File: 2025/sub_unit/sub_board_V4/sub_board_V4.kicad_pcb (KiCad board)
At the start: 2 copper layers, 66.8 x 58 mm, 38 parts, among them J1 Conn_01x02_Socket, J10 Conn_01x02_Socket, J11 Conn_01x03_Socket, J12 Conn_01x02_Socket, J13 Conn_01x02_Socket, J14 Conn_01x05_Socket, J15 Conn_01x05_Socket, J16 Conn_01x02_Socket, J18 Conn_01x07_Socket, J19 Conn_01x07_Socket, J2 Conn_01x02_Socket, J3 Conn_01x02_Socket, J4 Conn_01x02_Socket, J5 Conn_01x02_Socket, J6 Conn_01x02_Socket, J7 Conn_01x02_Socket, J8 Conn_01x02_Socket, J9 Conn_01x02_Socket

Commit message: 回路図変更
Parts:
- added J17: Conn_01x02_Socket, Connector_JST:JST_PH_B2B-PH-K_1x02_P2.00mm_Vertical, F.Cu at (25.6, -15.3)
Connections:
- J11 pad 1: DRI_SIGNAL -> GNDPWR
- J11 pad 3: GNDPWR -> +6V
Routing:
- net DRI_SIGNAL: track 59.3 -> 0.01 mm
- net GNDPWR: track 16.6 -> 24.1 mm
- net +6V: track 141.3 -> 147.8 mm

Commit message: PCB修正
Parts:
- moved J17 8.64 mm to (18.4, -10.7)
- moved D1 5.63 mm to (19.9, -18.8)
- moved R3 5.51 mm to (14.4, -16.2), turned to 0 degrees
- moved D2 5.42 mm to (19.9, -20.6)
- moved R1 3.10 mm to (14.3, -20.6)
- moved R4 3.08 mm to (14.3, -18.8)
- moved G*** 0.89 mm to (17.2, -17.4)
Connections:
- J19 pad 3: DRI_SIGNAL -> unconnected-(J19-Pin_3-Pad3)
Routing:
- net CANH: track 109.8 -> 131.7 mm
- net CANL: track 111.5 -> 130.8 mm
- net +6V: track 147.8 -> 160.9 mm
- net GNDPWR: track 24.1 -> 20.4 mm
- net Net-(D1-A): track 2.05 -> 5.03 mm
- net Net-(J13-Pin_1): track 8.80 -> 5.89 mm
- net Net-(D2-A): track 1.94 -> 4.73 mm
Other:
- board text added: "+15"
- board text added: "+6"
- board text added: "V4.0"
- board text removed: "+15V"
- board text removed: "+6V"
- board text removed: "V2.0"

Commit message: PCB修正2
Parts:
- moved J11 0.64 mm to (-18.6, -11.5)
- moved R2 0.59 mm to (-18.5, -20.4)
- moved R5 0.59 mm to (-14.9, -20.4)
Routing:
- net CANL: track 130.8 -> 132.6 mm
- net GNDPWR: track 20.4 -> 19.6 mm
- net Net-(J12-Pin_1): track 5.29 -> 4.70 mm
- net TR_SIGNAL: track 82.7 -> 82.1 mm

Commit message: PCB修正3
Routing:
- net +6V: track 161.0 -> 95.0 mm, vias 0 -> 1
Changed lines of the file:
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@@
-	)
-	(segment
-		(start 21.5 -16.55)
-		(end 20.45 -15.5)
-		(width 0.25)
-		(layer "F.Cu")
-		(net 8)
-	)
-	(segment
-		(start 19.3 -28.1)
-		(end 21.5 -25.9)
-		(width 0.25)
-		(layer "F.Cu")
-		(net 8)
-	)
-	(segment
-		(start 17.95 -7.3)
-		(end 22.6 -7.3)
-		(width 0.25)
-		(layer "F.Cu")
-		(net 8)
-	)
-	(segment
-		(start 26.15 8.55)
-		(end 19.233669 15.466331)
-		(width 0.25)
-		(layer "F.Cu")
-		(net 8)
 	)
 	(segment
 		(start 11.55 -6.35)
 		(end -11.684 -6.35)
-		(width 0.25)
-		(layer "F.Cu")
-		(net 8)
-	)
-	(segment
-		(start 1.9 12.1)
-		(end 0 14)
 		(width 0.25)
 		(layer "F.Cu")
@@
 	)
 	(segment
-		(start 26.15 -3.75)
-		(end 26.15 8.55)
-		(width 0.25)
-		(layer "F.Cu")
-		(net 8)
-	)
-	(segment
 		(start 0 19.812)
 		(end 0 23.92)
@@
 	)
 	(segment
-		(start 13.525 -25.875)
-		(end 15.75 -28.1)
-		(width 0.25)
-		(layer "F.Cu")
-		(net 8)
-	)
-	(segment
 		(start -11.684 -6.35)
 		(end -12.7 -7.366)
-		(width 0.25)
-		(layer "F.Cu")
-		(net 8)
-	)
-	(segment
-		(start 20.45 -15.5)
-		(end 17.65 -15.5)
 		(width 0.25)
 		(layer "F.Cu")
@@
 	)
 	(segment
-		(start 19.233669 15.466331)
-		(end 14.666331 15.466331)
-		(width 0.25)
-		(layer "F.Cu")
-		(net 8)
-	)
-	(segment
 		(start -12.7 -19.25)
 		(end -13.85 -20.4)
-		(width 0.25)
-		(layer "F.Cu")
-		(net 8)
-	)
-	(segment
-		(start 11.3 12.1)
-		(end 1.9 12.1)
 		(width 0.25)
 		(layer "F.Cu")
@@
 		(end 0 14)
 		(width 1.5)
-		(layer "F.Cu")
-		(net 8)
-	)
-	(segment
-		(start 17.65 -15.5)
-		(end 16.5 -14.35)
-		(width 0.25)
-		(layer "F.Cu")
-		(net 8)
-	)
-	(segment
-		(start 22.6 -7.3)
-		(end 26.15 -3.75)
-		(width 0.25)
 		(layer "F.Cu")
 		(net 8)
@@
 		(start -17.998 -16.5)
 		(end -18.6 -16.5)
-		(width 0.25)
-		(layer "F.Cu")
-		(net 8)
-	)
-	(segment
-		(start 21.5 -25.9)
-		(end 21.5 -16.55)
-		(width 0.25)
-		(layer "F.Cu")
-		(net 8)
-	)
-	(segment
-		(start 16.5 -14.35)
-		(end 16.5 -8.75)
 		(width 0.25)
 		(layer "F.Cu")
@@
 		(net 8)
 	)
-	(segment
-		(start 16.5 -8.75)
-		(end 17.95 -7.3)
-		(width 0.25)
-		(layer "F.Cu")
+	(via
+		(at -11.684 -6.35)
+		(size 0.8)
+		(drill 0.4)
+		(layers "F.Cu" "B.Cu")
 		(net 8)
 	)
 	(segment
-		(start 15.75 -28.1)
-		(end 19.3 -28.1)
+		(start -10.05 1.9)
+		(end -5.35 6.6)
 		(width 0.25)
-		(layer "F.Cu")
+		(layer "B.Cu")
 		(net 8)
 	)
 	(segment
-		(start 13.525 -20.6)
-		(end 13.525 -25.875)
+		(start 0 14)
+		(end 0 13.535176)
 		(width 0.25)
-		(layer "F.Cu")
+		(layer "B.Cu")
 		(net 8)
 	)
 	(segment
-		(start 14.666331 15.466331)
-		(end 11.3 12.1)
+		(start -5.35 6.6)
+		(end -5.35 8.185176)
 		(width 0.25)
-		(layer "F.Cu")
+		(layer "B.Cu")
 		(net 8)
 	)
+	(segment
+		(start -5.35 8.185176)
+		(end 0 13.535176)
+		(width 0.25)
+		(layer "B.Cu")
+		(net 8)
+	)
+	(segment
+		(start -11.684 -6.35)
+		(end -10.05 -4.716)
+		(width 0.25)
+		(layer "B.Cu")
+		(net 8)
+	)
+	(segment
+		(start -10.05 -4.716)
+		(end -10.05 1.9)
+		(width 0.25)
+		(layer "B.Cu")
+		(net 8)
+	)

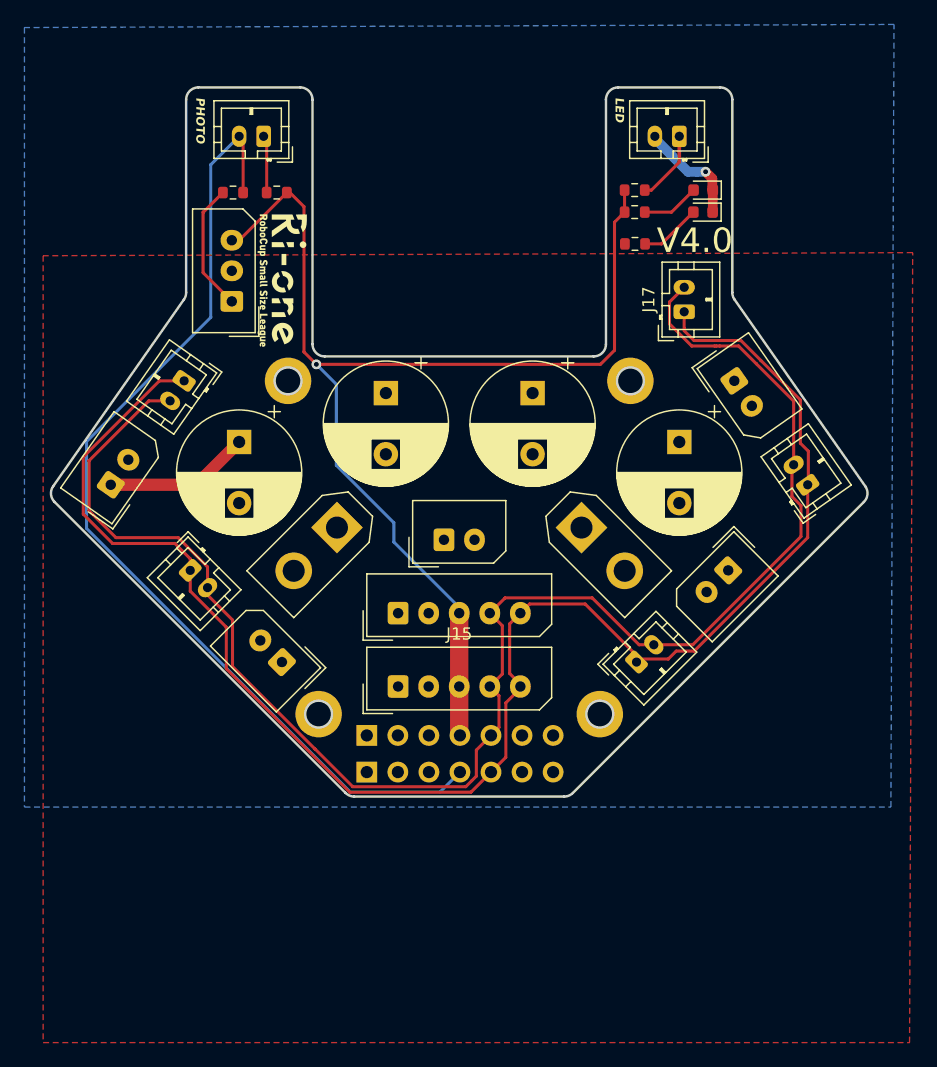
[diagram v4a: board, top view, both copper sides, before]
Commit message: 完成、製造データ出力
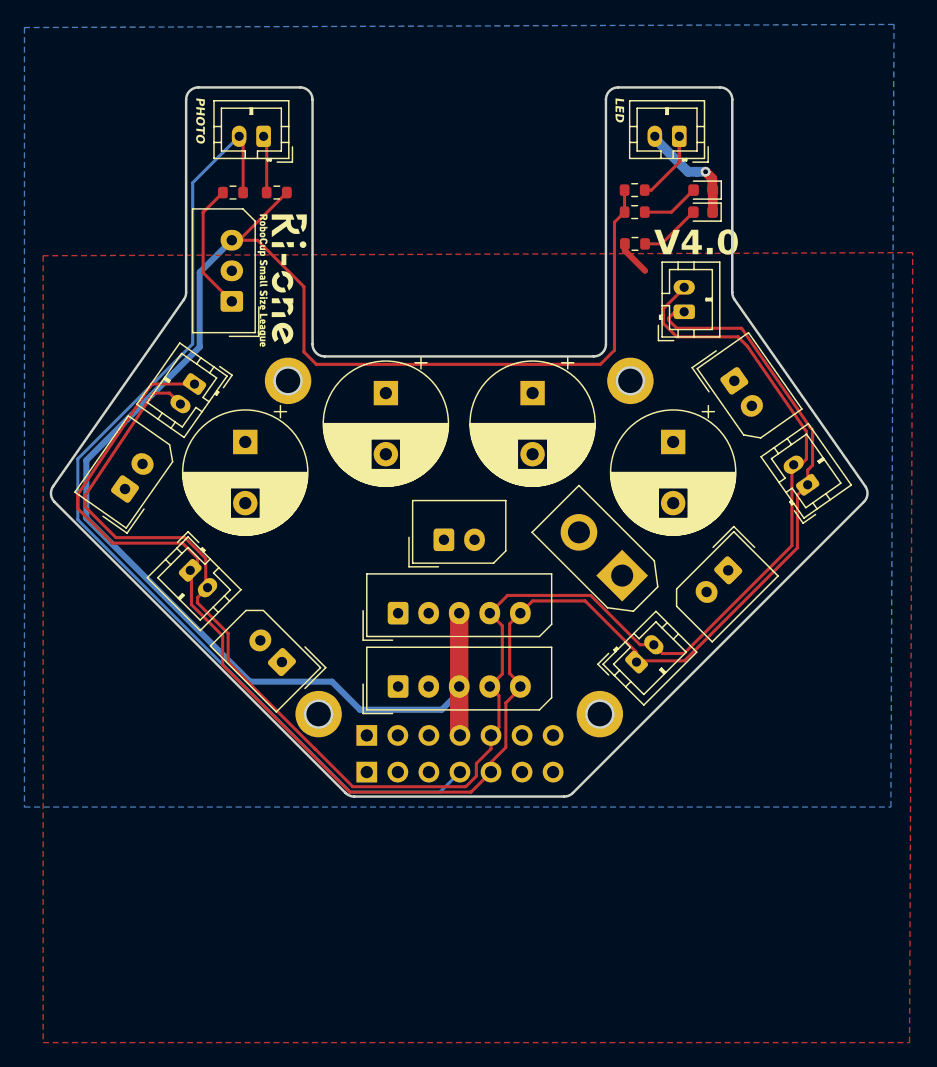
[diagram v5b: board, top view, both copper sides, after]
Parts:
- removed ? (x4): , 
- removed J9: Conn_01x02_Socket, Connector_AMASS:AMASS_XT30UPB-M_1x02_P5.0mm_Vertical
- added H1: MountingHole, MountingHole:MountingHole_2.2mm_M2_DIN965_Pad, F.Cu at (-14.0, -5.00)
- added H2: MountingHole, MountingHole:MountingHole_2.2mm_M2_DIN965_Pad, F.Cu at (14.0, -5.00)
- added H3: MountingHole, MountingHole:MountingHole_2.2mm_M2_DIN965_Pad, F.Cu at (-11.5, 22.3)
- added H4: MountingHole, MountingHole:MountingHole_2.2mm_M2_DIN965_Pad, F.Cu at (11.5, 22.3)
- moved J10 5.15 mm to (13.3, 10.9), turned to 135 degrees
- moved J5 1.22 mm to (-27.3, 3.85)
- moved J1 0.89 mm to (-21.7, -4.74)
- moved C2 0.50 mm to (17.5, 0.00)
- moved C3 0.50 mm to (-17.5, 0.00)
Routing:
- net +6V: track 95.0 -> 134.6 mm, vias 1 -> 0
- net +15V: track 11.9 -> 2.88 mm
- net CANH: track 131.9 -> 136.1 mm
- net CANL: track 132.6 -> 136.5 mm
- net TR_SIGNAL: track 82.1 -> 82.7 mm
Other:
- board text added: "SubBoardVer4.0 20250116"
- board text removed: "SubBoardVer2.0 20240606 KotaroOCHIISHI"

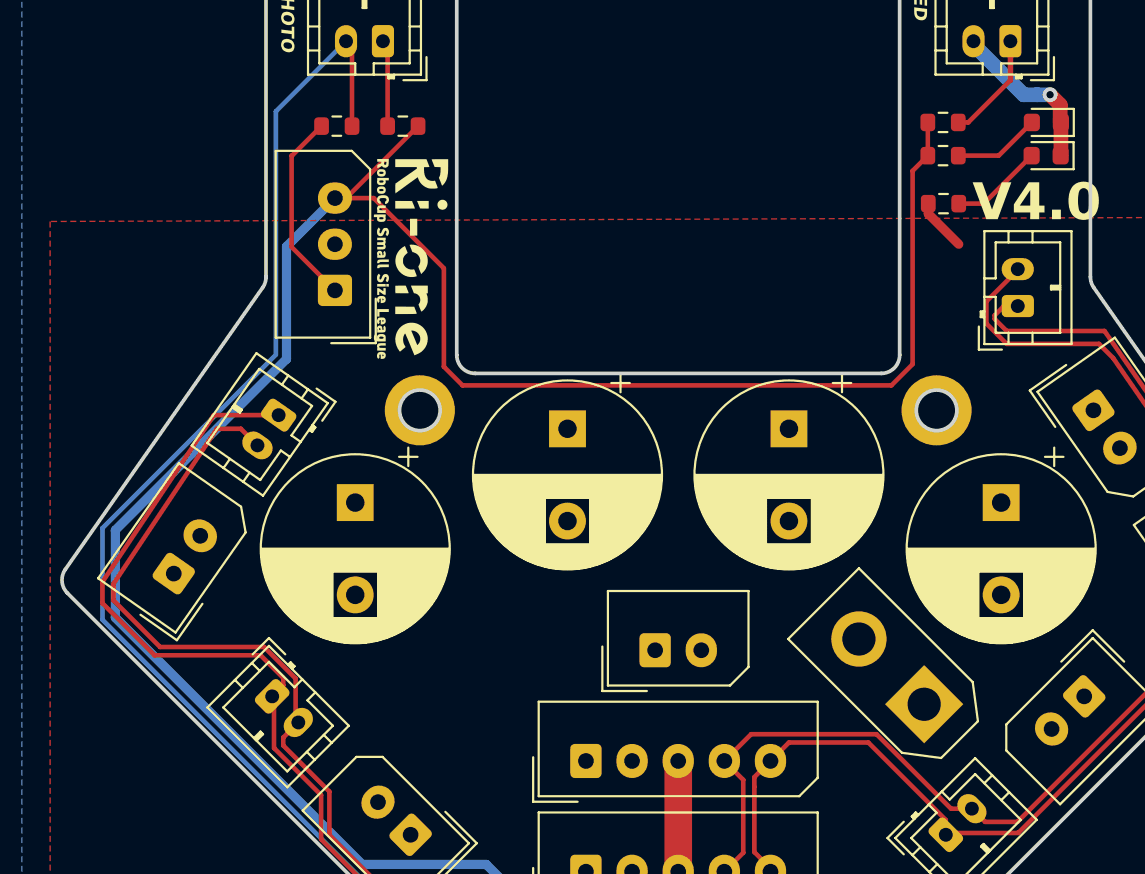
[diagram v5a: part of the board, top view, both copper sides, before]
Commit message: ドリブラー用コネクタのピン配置変更
製造データ再出力
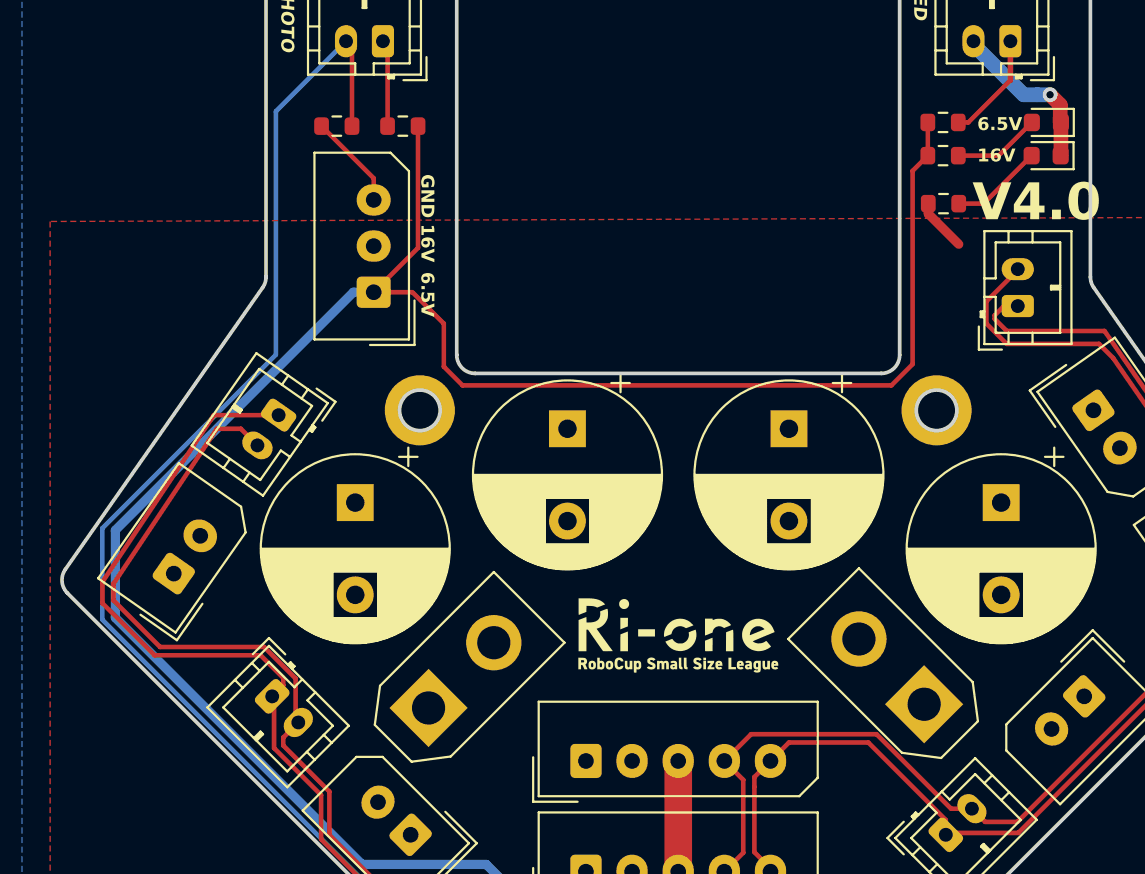
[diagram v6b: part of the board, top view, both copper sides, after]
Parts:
- removed J16: Conn_01x02_Socket, Connector_Molex:Molex_SPOX_5267-02A_1x02_P2.50mm_Vertical
- added J9: Conn_01x02_Socket, Connector_AMASS:AMASS_XT30UPB-M_1x02_P5.0mm_Vertical, F.Cu at (-13.5, 11.1)
- moved G*** 25.0 mm to (0.00, 7.20), turned to 0 degrees
- moved J11 2.10 mm to (-16.5, -11.4)
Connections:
- J11 pad 1: GNDPWR -> +6V
- J11 pad 3: +6V -> GNDPWR
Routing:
- net +6V: track 134.6 -> 128.8 mm
- net GNDPWR: track 19.6 -> 14.2 mm
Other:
- board text added: "16V"
- board text added: "6.5V"
- board text added: "GND"
- board text removed: "+15"
- board text removed: "+6"

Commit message: 抵抗値の変更、ibomの生成
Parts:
- D1: value LED -> LED_Red
- D2: value LED -> LED_Blue
- R2: value 20k -> 2.2k
- R3: value 20k -> 10k
- R4: value 2k -> 2.2k
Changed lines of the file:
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@@
 			)
 		)
-		(property "Value" "LED"
+		(property "Value" "LED_Blue"
 			(at 0 1.43 0)
 			(layer "F.Fab")
@@
 			)
 		)
-		(property "Value" "20k"
+		(property "Value" "2.2k"
 			(at 0 1.43 0)
 			(layer "F.Fab")
@@
 			)
 		)
-		(property "Value" "LED"
+		(property "Value" "LED_Red"
 			(at 0 1.43 0)
 			(layer "F.Fab")
@@
 			)
 		)
-		(property "Value" "2k"
+		(property "Value" "2.2k"
 			(at 0.05 1.3 0)
 			(layer "F.Fab")
@@
 			)
 		)
-		(property "Value" "20k"
+		(property "Value" "10k"
 			(at 2.75 0.1 0)
 			(layer "F.Fab")
